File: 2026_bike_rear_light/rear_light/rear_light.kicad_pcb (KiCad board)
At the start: 2 copper layers, 23 parts, among them J1 Conn_01x04, J2 Conn_01x05, Q1 2N5551, Q2 FQP27P06, Q3 2N5551, Q4 FQP27P06, Q5 2N5551, Q6 2N5551, Q7 FQP27P06, U1 LM2596HV

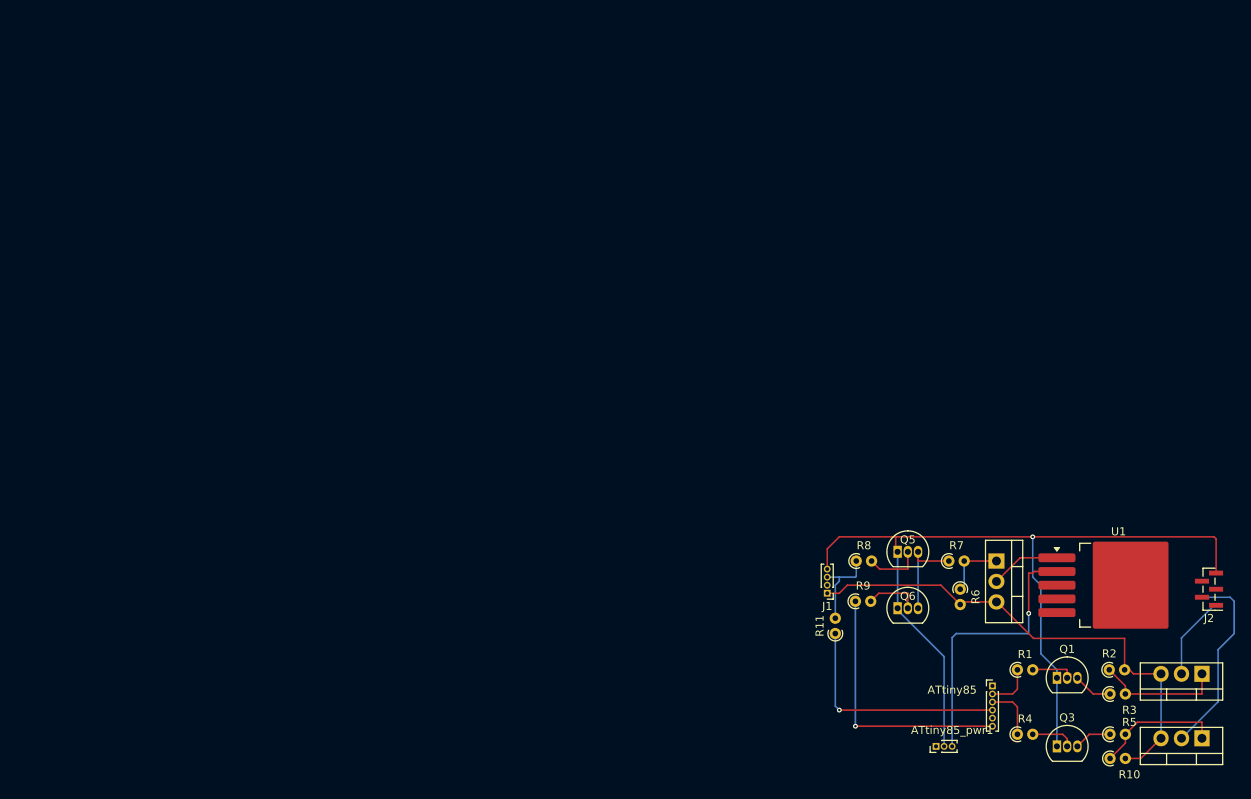
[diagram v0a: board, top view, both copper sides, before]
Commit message: Bike Rear Light - pcb layout, this time with modules and for hand soldering
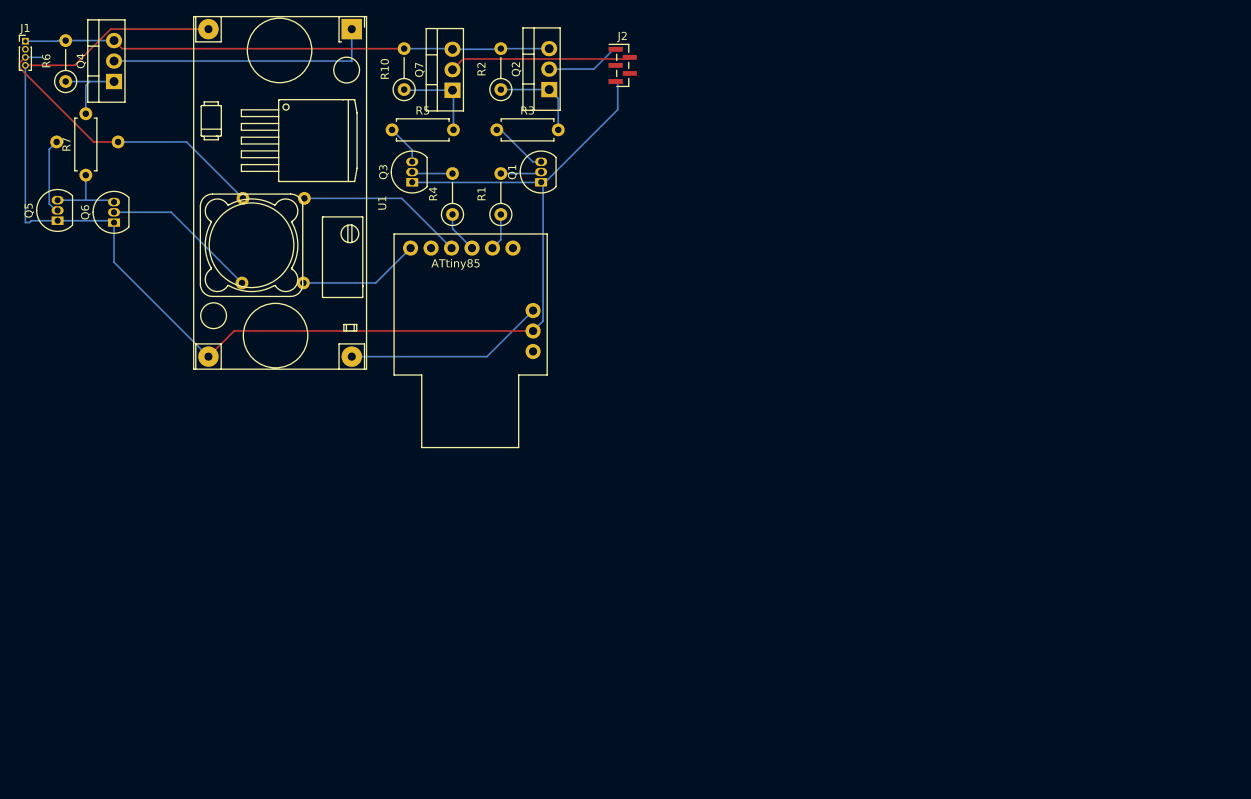
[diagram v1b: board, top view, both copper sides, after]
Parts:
- removed ATtiny85_pwr1: Conn_01x03, Connector_PinHeader_1.00mm:PinHeader_1x03_P1.00mm_Vertical
- ATtiny85: value Conn_01x06 -> Conn_01x09; footprint Connector_PinHeader_1.00mm:PinHeader_1x06_P1.00mm_Vertical -> models:Digispark
- R1, R10, R2, R4, R6: footprint Resistor_THT:R_Axial_DIN0204_L3.6mm_D1.6mm_P1.90mm_Vertical -> Resistor_THT:R_Axial_DIN0207_L6.3mm_D2.5mm_P5.08mm_Vertical
- R11, R8, R9: footprint Resistor_THT:R_Axial_DIN0204_L3.6mm_D1.6mm_P1.90mm_Vertical -> Resistor_THT:R_Axial_DIN0207_L6.3mm_D2.5mm_P7.62mm_Horizontal; moved to B.Cu
- R3, R5, R7: footprint Resistor_THT:R_Axial_DIN0204_L3.6mm_D1.6mm_P1.90mm_Vertical -> Resistor_THT:R_Axial_DIN0207_L6.3mm_D2.5mm_P7.62mm_Horizontal
- U1: value LM2596HV -> YAAJ_DCDC_StepDown_LM2596; footprint Package_TO_SOT_SMD:TO-263-5_TabPin3 -> models:YAAJ_DCDC_StepDown_LM2596
- moved R6 127.6 mm to (66.0, 53.5), turned to 90 degrees
- moved Q4 124.6 mm to (72.0, 53.5), turned to 90 degrees
- moved Q7 122.9 mm to (114.0, 54.6), turned to 90 degrees
- moved J1 120.8 mm to (61.0, 48.5), turned to 0 degrees
- moved R10 120.7 mm to (108.0, 54.5), turned to 90 degrees
- moved U1 117.5 mm to (101.5, 47.0), turned to -90 degrees
- moved R7 117.3 mm to (68.5, 65.1), turned to 90 degrees
- moved R5 116.5 mm to (106.5, 59.5)
- moved Q5 112.0 mm to (65.0, 70.8), turned to 90 degrees
- moved Q2 108.7 mm to (126.0, 54.5), turned to 90 degrees
- moved Q6 108.4 mm to (72.0, 71.0), turned to 90 degrees
- moved Q3 106.3 mm to (109.0, 66.0), turned to 90 degrees
- moved R8 105.3 mm to (72.5, 61.0), turned to 180 degrees
- moved R2 104.3 mm to (120.0, 54.5), turned to 90 degrees
- moved R3 103.4 mm to (119.5, 59.5)
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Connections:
- U1 pad 2: VIN -> GND
- U1 pad 4: unconnected-(U1-FB-Pad4) -> VIN
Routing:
- net GND: track 112.0 -> 170.4 mm, vias 1 -> 0
- net +5V: track 10.8 -> 38.1 mm
- net Net-(Q4-D): track 8.72 -> 33.5 mm
- net /PB5: track 32.5 -> 15.1 mm, vias 1 -> 0
- net Net-(Q6-B): track 6.87 -> 19.5 mm
- net VIN: track 34.3 -> 24.9 mm, vias 1 -> 0
- net /PB3: track 28.7 -> 20.8 mm, vias 1 -> 0
- net Net-(Q7-G): track 15.9 -> 11.0 mm
- net Net-(Q2-G): track 15.8 -> 11.5 mm
- net +48V: track 63.0 -> 65.5 mm
- net Net-(Q5-B): track 7.05 -> 9.45 mm
- net Net-(Q1-C): track 4.91 -> 7.14 mm
- net Net-(Q5-C): track 12.0 -> 10.2 mm
- net /BRAKE_LIGHT: track 6.75 -> 5.17 mm
- net /BRAKE: track 23.9 -> 22.6 mm
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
